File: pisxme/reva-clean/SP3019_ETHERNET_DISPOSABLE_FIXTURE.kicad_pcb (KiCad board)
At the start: 6 copper layers, 300 x 180 mm, 4 parts, among them J2 A70-112-331N126, J7 Raspberry-Pi-5-Compute-Module, U6 SP3019-04HTG, U9 SP3019-04HTG

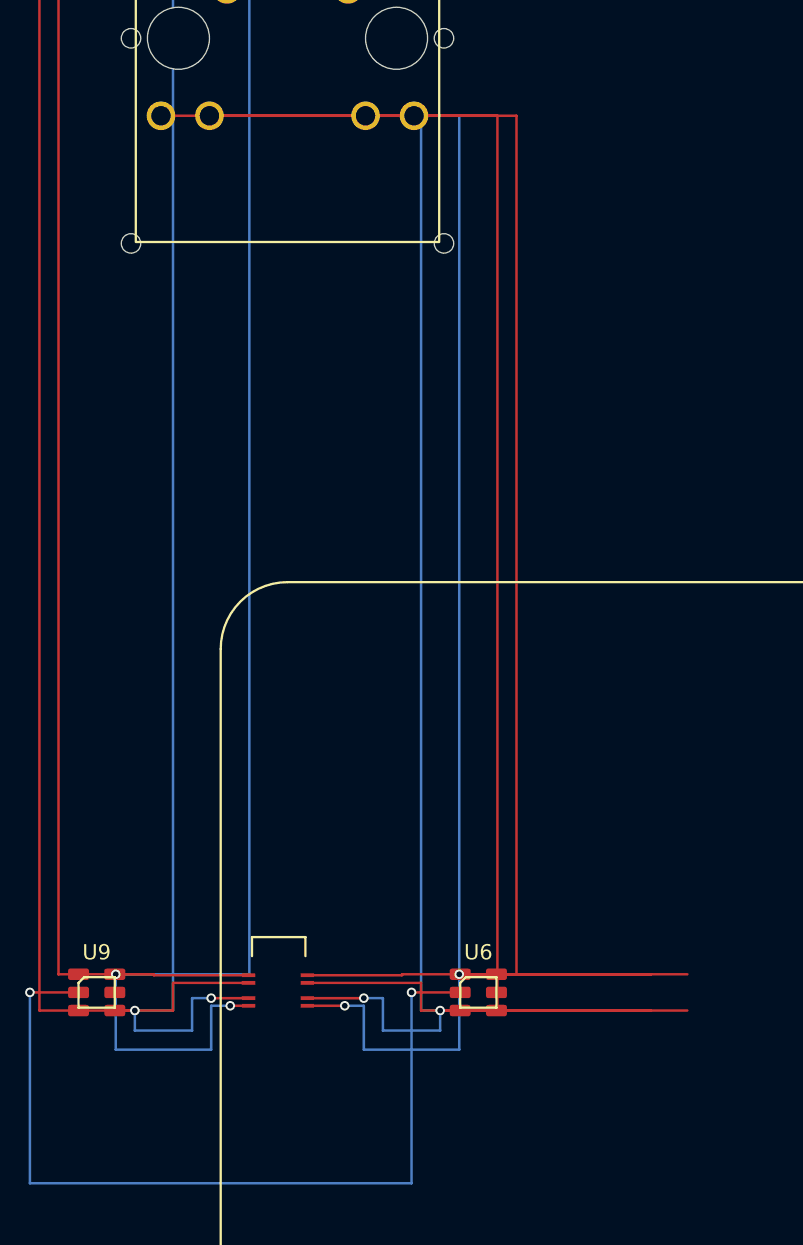
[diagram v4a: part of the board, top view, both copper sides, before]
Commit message: phase17: separate Ethernet source fanout
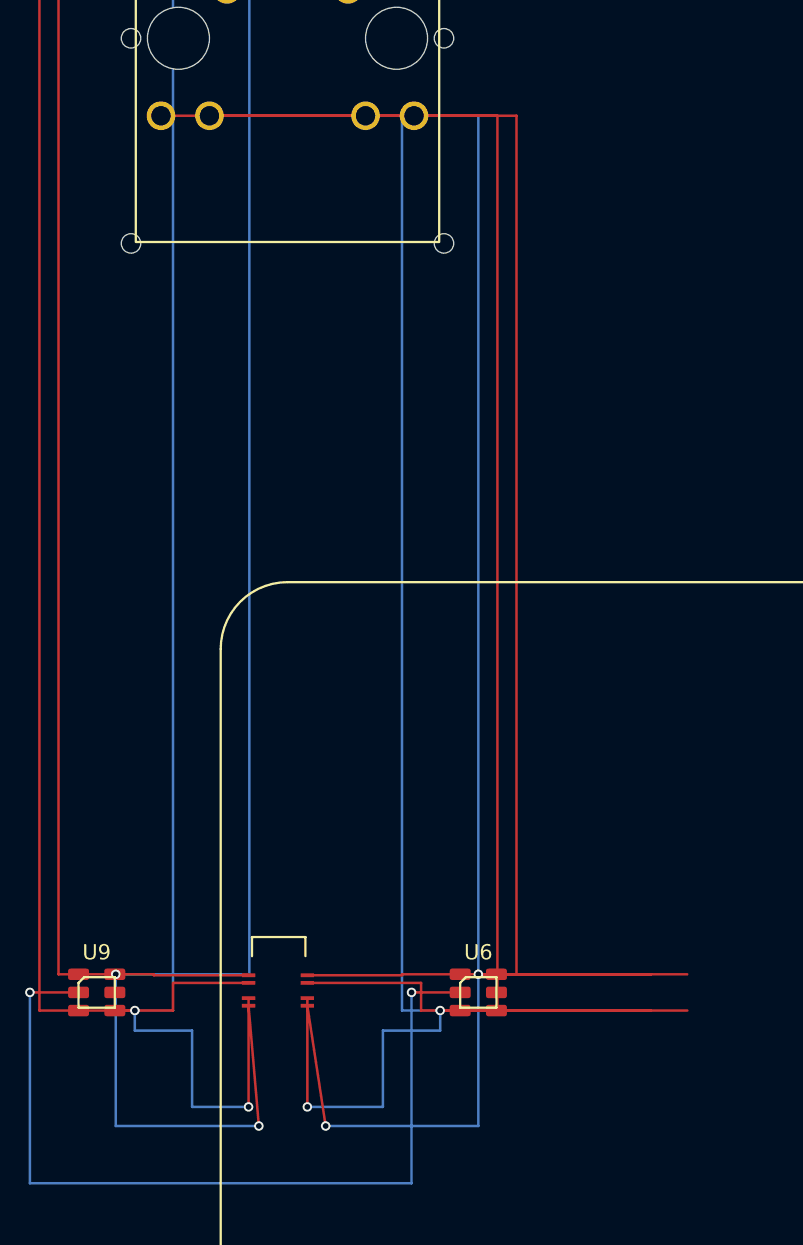
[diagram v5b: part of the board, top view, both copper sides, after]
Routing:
- net CM5_GBE_TD2_P: track 80.9 -> 89.4 mm
- net CM5_GBE_TD0_P: track 73.5 -> 81.6 mm
- net CM5_GBE_TD2_N: track 74.4 -> 82.4 mm
- net CM5_GBE_TD0_N: track 73.5 -> 81.5 mm
